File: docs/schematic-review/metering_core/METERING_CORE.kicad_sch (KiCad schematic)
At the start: 56 parts, among them U2 ATM90E26-YU, U4 ISO6721BD, U5 MAX3487E

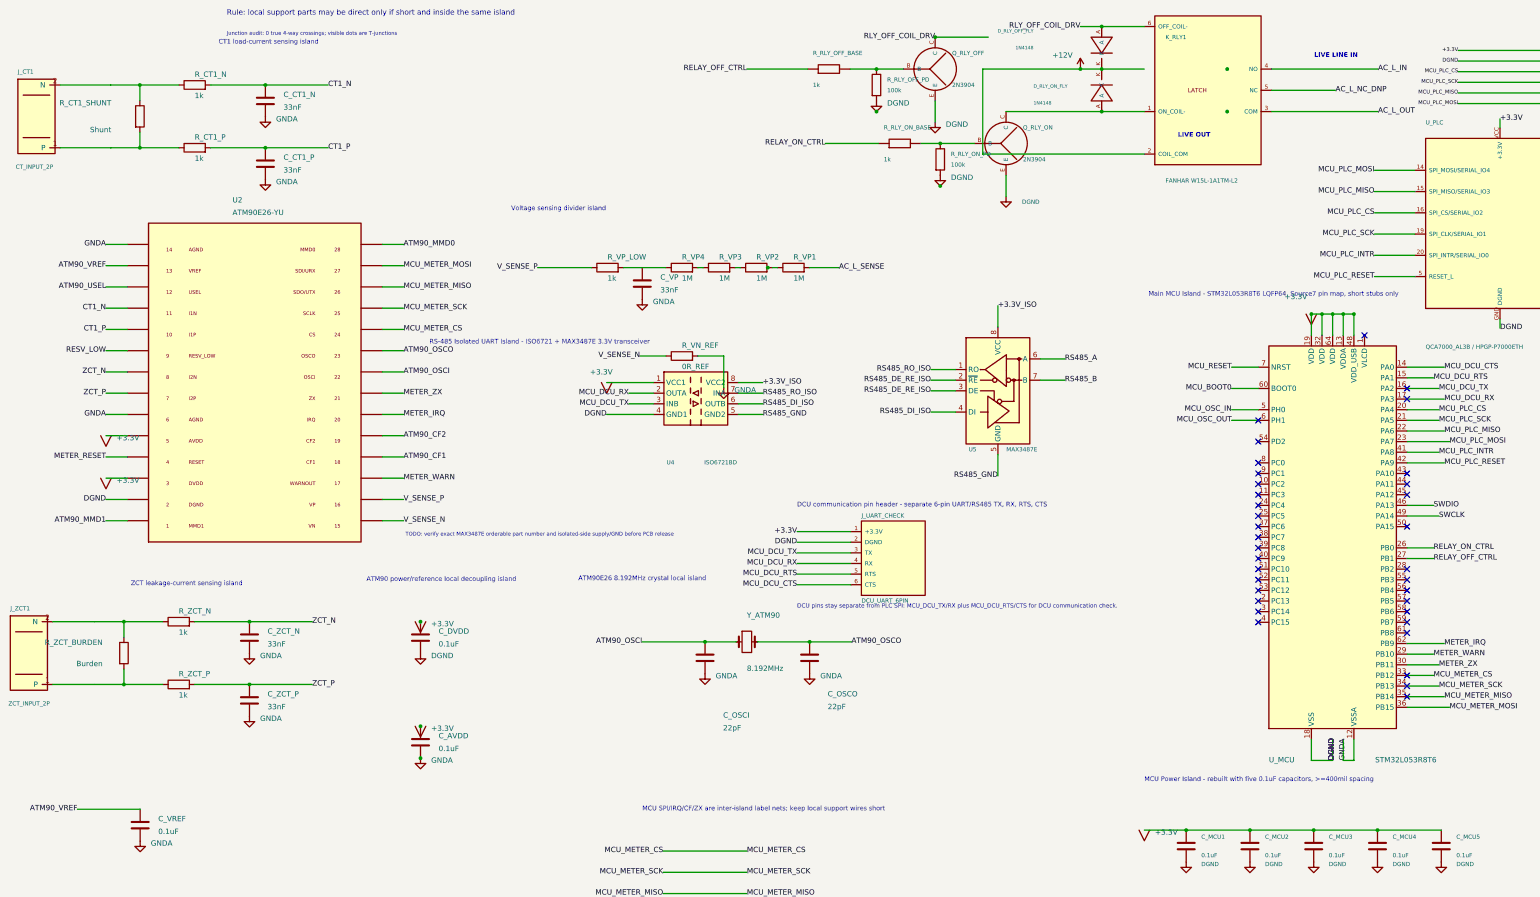
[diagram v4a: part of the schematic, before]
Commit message: Fix metering schematic visual clearance hot spots
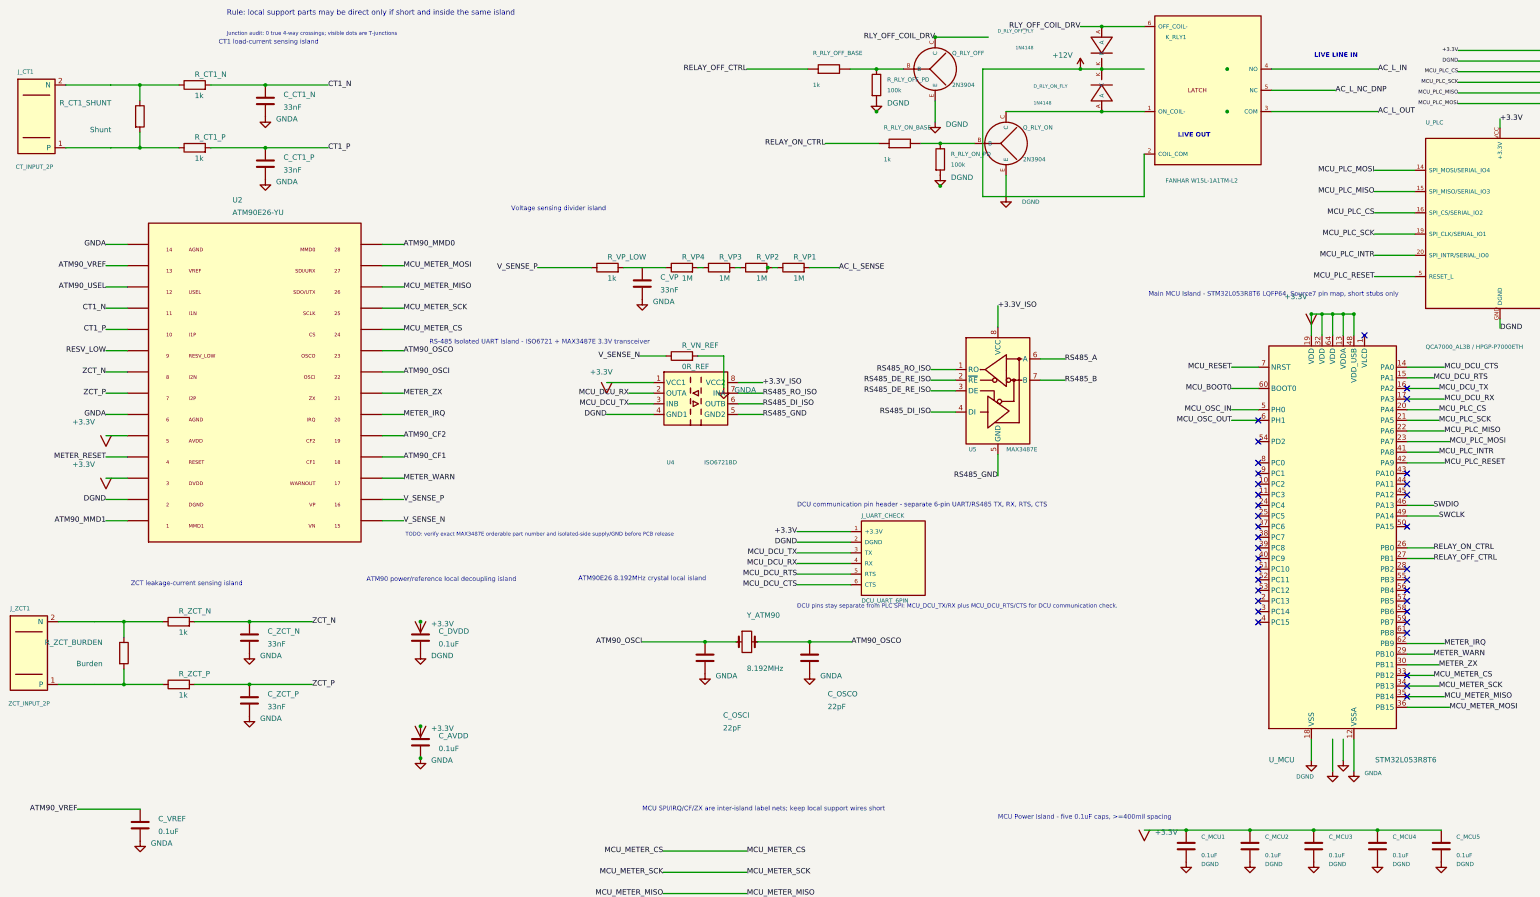
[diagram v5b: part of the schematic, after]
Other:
- note added: "MCU Power Island - five 0.1uF caps, >=400mil spacing"
- note removed: "MCU Power Island - rebuilt with five 0.1uF capacitors, >=400mil spacing"
- moved on the sheet: J_CT1, J_ZCT1
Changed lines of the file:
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@@
 		(company "IOTECH")
 	)
-	(text "MCU Power Island - rebuilt with five 0.1uF capacitors, >=400mil spacing"
+	(text "MCU Power Island - five 0.1uF caps, >=400mil spacing"
 		(exclude_from_sim no)
-		(at 285 208 0)
+		(at 250 217 0)
 		(effects
 			(font
@@
 	(wire
 		(pts
-			(xy 330 198.26) (xy 330 203.34)
+			(xy 330 198.26) (xy 330 205.88)
 		)
 		(stroke
@@
 	(wire
 		(pts
-			(xy 324.92 203.34) (xy 330 203.34)
-		)
-		(stroke
-			(width 0)
-			(type solid)
-		)
-	)
-	(wire
-		(pts
 			(xy 102.87 95.25) (xy 107.95 95.25)
 		)
@@
 	(wire
 		(pts
-			(xy 335.08 198.26) (xy 335.08 203.34)
+			(xy 335.08 198.26) (xy 335.08 205.88)
 		)
 		(stroke
@@
 		)
 	)
-	(wire
-		(pts
-			(xy 332.54 203.34) (xy 335.08 203.34)
+	(symbol
+		(lib_id "power:DGND")
+		(at 324.92 203.34 0)
+		(unit 1)
+		(body_style 1)
+		(exclude_from_sim no)
+		(in_bom yes)
+		(on_board yes)
+		(in_pos_files yes)
+		(dnp no)
+		(property "Reference" "#PWR_MCU_BOTTOM_DGND1"
+			(at 327.46 199.53 0)
+			(hide yes)
+			(show_name no)
+			(do_not_autoplace no)
+			(effects (font (size 1.27 1.27)))
 		)
-		(stroke
-			(width 0)
-			(type solid)
+		(property "Value" "DGND"
+			(at 321.3 207.2 0)
+			(show_name no)
+			(do_not_autoplace no)
+			(effects (font (size 1.0 1.0)) (justify left))
 		)
+		(property "Footprint" "" (at 324.92 203.34 0) (show_name no) (do_not_autoplace no) (effects (font (size 1.27 1.27))))
+		(property "Datasheet" "" (at 324.92 203.34 0) (show_name no) (do_not_autoplace no) (effects (font (size 1.27 1.27))))
+		(property "Description" "" (at 324.92 203.34 0) (show_name no) (do_not_autoplace no) (effects (font (size 1.27 1.27))))
+		(pin "1")
+		(instances (project "METERING_CORE" (path "/e4236fbb-ccab-4d10-bcea-7fda722d6751" (reference "#PWR_MCU_BOTTOM_DGND1") (unit 1))))
+	)
+	(symbol
+		(lib_id "power:DGND")
+		(at 330 205.88 0)
+		(unit 1)
+		(body_style 1)
+		(exclude_from_sim no)
+		(in_bom yes)
+		(on_board yes)
+		(in_pos_files yes)
+		(dnp no)
+		(property "Reference" "#PWR_MCU_BOTTOM_DGND2" (at 332.54 202.07 0) (hide yes) (show_name no) (do_not_autoplace no) (effects (font (size 1.27 1.27))))
+		(property "Value" "DGND" (at 332.54 206.388 0) (hide yes) (show_name no) (do_not_autoplace no) (effects (font (size 1.0 1.0)) (justify left)))
+		(property "Footprint" "" (at 330 205.88 0) (show_name no) (do_not_autoplace no) (effects (font (size 1.27 1.27))))
+		(property "Datasheet" "" (at 330 205.88 0) (show_name no) (do_not_autoplace no) (effects (font (size 1.27 1.27))))
+		(property "Description" "" (at 330 205.88 0) (show_name no) (do_not_autoplace no) (effects (font (size 1.27 1.27))))
+		(pin "1")
+		(instances (project "METERING_CORE" (path "/e4236fbb-ccab-4d10-bcea-7fda722d6751" (reference "#PWR_MCU_BOTTOM_DGND2") (unit 1))))
+	)
+	(symbol
+		(lib_id "power:GNDA")
+		(at 332.54 203.34 0)
+		(unit 1)
+		(body_style 1)
+		(exclude_from_sim no)
+		(in_bom yes)
+		(on_board yes)
+		(in_pos_files yes)
+		(dnp no)
+		(property "Reference" "#PWR_MCU_BOTTOM_GNDA1" (at 335.08 199.53 0) (hide yes) (show_name no) (do_not_autoplace no) (effects (font (size 1.27 1.27))))
+		(property "Value" "GNDA" (at 335.1 202.3 0) (hide yes) (show_name no) (do_not_autoplace no) (effects (font (size 1.0 1.0)) (justify left)))
+		(property "Footprint" "" (at 332.54 203.34 0) (show_name no) (do_not_autoplace no) (effects (font (size 1.27 1.27))))
+		(property "Datasheet" "" (at 332.54 203.34 0) (show_name no) (do_not_autoplace no) (effects (font (size 1.27 1.27))))
+		(property "Description" "" (at 332.54 203.34 0) (show_name no) (do_not_autoplace no) (effects (font (size 1.27 1.27))))
+		(pin "1")
+		(instances (project "METERING_CORE" (path "/e4236fbb-ccab-4d10-bcea-7fda722d6751" (reference "#PWR_MCU_BOTTOM_GNDA1") (unit 1))))
+	)
+	(symbol
+		(lib_id "power:GNDA")
+		(at 335.08 205.88 0)
+		(unit 1)
+		(body_style 1)
+		(exclude_from_sim no)
+		(in_bom yes)
+		(on_board yes)
+		(in_pos_files yes)
+		(dnp no)
+		(property "Reference" "#PWR_MCU_BOTTOM_GNDA2" (at 337.62 202.07 0) (hide yes) (show_name no) (do_not_autoplace no) (effects (font (size 1.27 1.27))))
+		(property "Value" "GNDA" (at 337.62 206.388 0) (show_name no) (do_not_autoplace no) (effects (font (size 1.0 1.0)) (justify left)))
+		(property "Footprint" "" (at 335.08 205.88 0) (show_name no) (do_not_autoplace no) (effects (font (size 1.27 1.27))))
+		(property "Datasheet" "" (at 335.08 205.88 0) (show_name no) (do_not_autoplace no) (effects (font (size 1.27 1.27))))
+		(property "Description" "" (at 335.08 205.88 0) (show_name no) (do_not_autoplace no) (effects (font (size 1.27 1.27))))
+		(pin "1")
+		(instances (project "METERING_CORE" (path "/e4236fbb-ccab-4d10-bcea-7fda722d6751" (reference "#PWR_MCU_BOTTOM_GNDA2") (unit 1))))
 	)
 	(wire
@@
 		)
 	)
-	(label "DGND"
-		(at 330 203.34 90)
-		(effects
-			(font
-				(size 1.27 1.27)
-			)
-		)
-	)
 	(label "METER_WARN"
 		(at 190 265.64 0)
@@
 		)
 	)
-	(label "DGND"
-		(at 330 203.34 90)
-		(effects
-			(font
-				(size 1.27 1.27)
-			)
-		)
-	)
 	(label "METER_ZX"
 		(at 355.4 180.48 0)
@@
 		)
 	)
-	(label "DGND"
-		(at 330 203.34 90)
-		(effects
-			(font
-				(size 1.27 1.27)
-			)
-		)
-	)
 	(label "ATM90_CF2"
 		(at 107.95 125.73 0)
@@
 		)
 		(property "Value" "+3.3V"
-			(at 39.37 136.398 0)
+			(at 34.2 132.6 0)
 			(show_name no)
 			(do_not_autoplace no)
-			(effects (font (size 1.27 1.27)) (justify left))
+			(effects (font (size 1.27 1.27)) (justify right))
 		)
 		(property "Footprint" ""
@@
 		)
 		(property "Value" "+3.3V"
-			(at 39.37 126.238 0)
+			(at 34.2 122.44 0)
 			(show_name no)
 			(do_not_autoplace no)
-			(effects (font (size 1.27 1.27)) (justify left))
+			(effects (font (size 1.27 1.27)) (justify right))
 		)
 		(property "Footprint" ""
@@
 		)
 	)
-	(label "GNDA"
-		(at 332.54 203.34 90)
-		(effects
-			(font
-				(size 1.27 1.27)
-			)
-		)
-	)
 	(label "CT1_N"
 		(at 36.83 95.25 180)
@@
 		)
 	)
-	(label "DGND"
-		(at 330 203.34 90)
-		(effects
-			(font
-				(size 1.27 1.27)
-			)
-		)
-	)
 	(label "MCU_BOOT0"
 		(at 305.87 114.44 180)
@@
 	(wire
 		(pts
-			(xy 246.38 58.42) (xy 284.96 58.42)
+			(xy 284.96 58.42) (xy 284.96 68.58)
+		)
+		(stroke
+			(width 0)
+			(type solid)
+		)
+	)
+	(wire
+		(pts
+			(xy 284.96 68.58) (xy 246.38 68.58)
+		)
+		(stroke
+			(width 0)
+			(type solid)
+		)
+	)
+	(wire
+		(pts
+			(xy 246.38 68.58) (xy 246.38 58.42)
 		)
 		(stroke
@@
 	(wire
 		(pts
-			(xy 25.93 41.91) (xy 37.93 41.91)
+			(xy 27.20 41.91) (xy 37.93 41.91)
 		)
 		(stroke
@@
 	(wire
 		(pts
-			(xy 25.93 56.91) (xy 37.93 56.91)
+			(xy 27.20 56.91) (xy 37.93 56.91)
 		)
 		(stroke
@@
 	(wire
 		(pts
-			(xy 24.12 170.18) (xy 34.12 170.18)
+			(xy 25.39 170.18) (xy 34.12 170.18)
 		)
 		(stroke
@@
 	(wire
 		(pts
-			(xy 24.12 185.18) (xy 34.12 185.18)
+			(xy 25.39 185.18) (xy 34.12 185.18)
 		)
 		(stroke

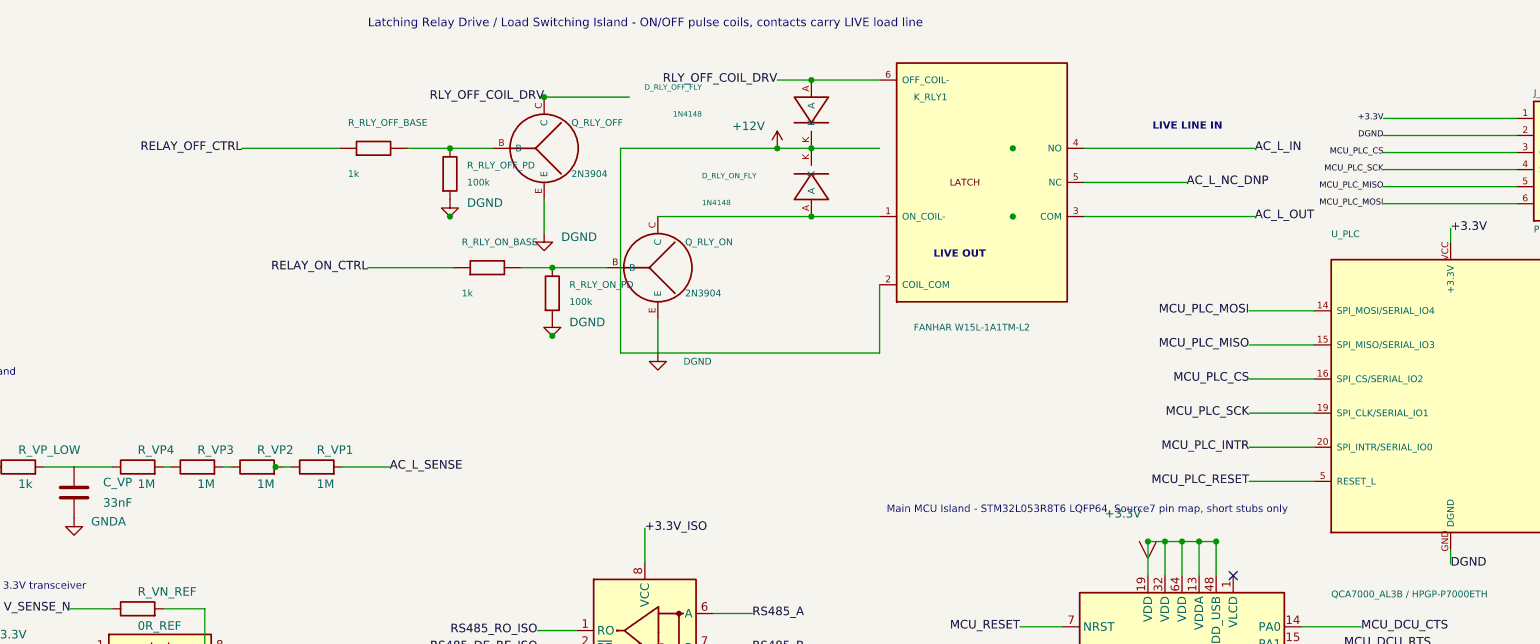
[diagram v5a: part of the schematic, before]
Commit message: Fix relay and MCU schematic visual clearance
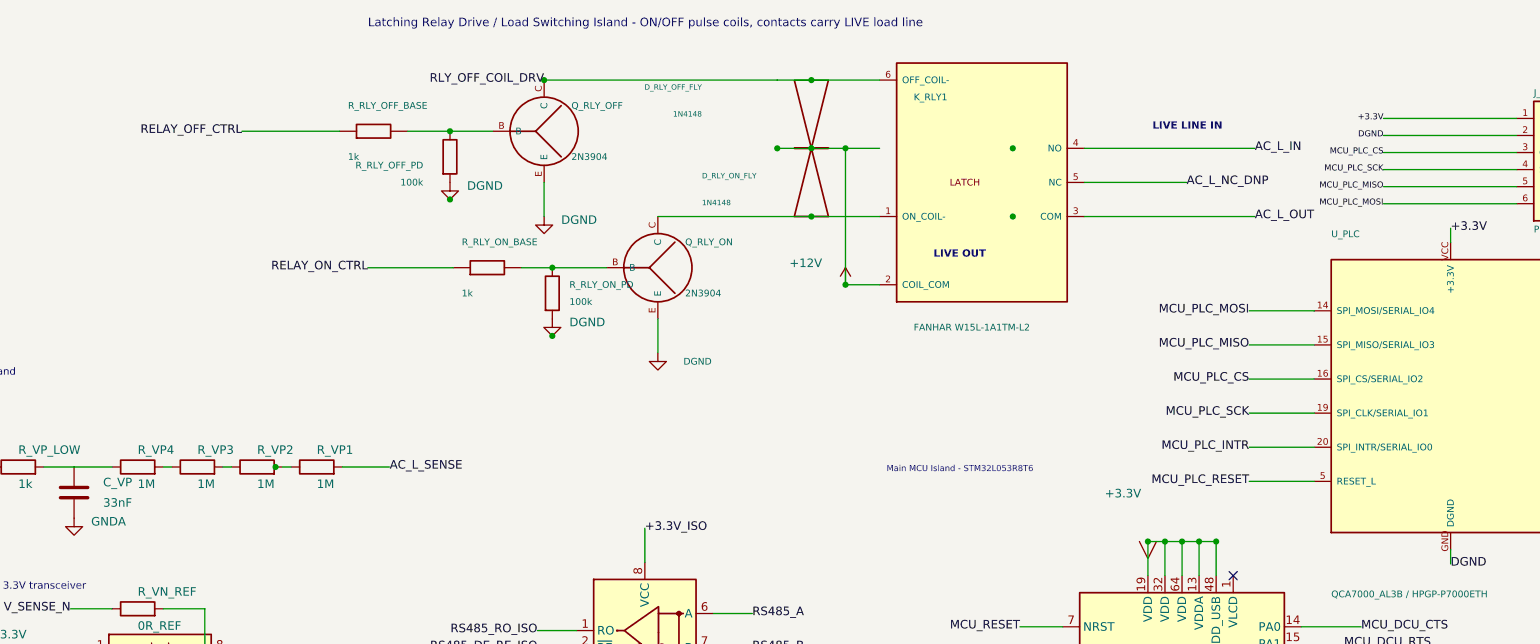
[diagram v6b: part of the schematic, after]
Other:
- note added: "Main MCU Island - STM32L053R8T6"
- note removed: "Main MCU Island - STM32L053R8T6 LQFP64, Source7 pin map, short stubs only"
- moved on the sheet: Q_RLY_OFF, R_RLY_OFF_BASE, R_RLY_OFF_PD
